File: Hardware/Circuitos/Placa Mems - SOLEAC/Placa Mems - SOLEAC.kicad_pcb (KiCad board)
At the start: 2 copper layers, 50 x 40 mm, 7 parts, among them J2 Conn_01x04, J6 Conn_01x02, Y1 MA40S4R

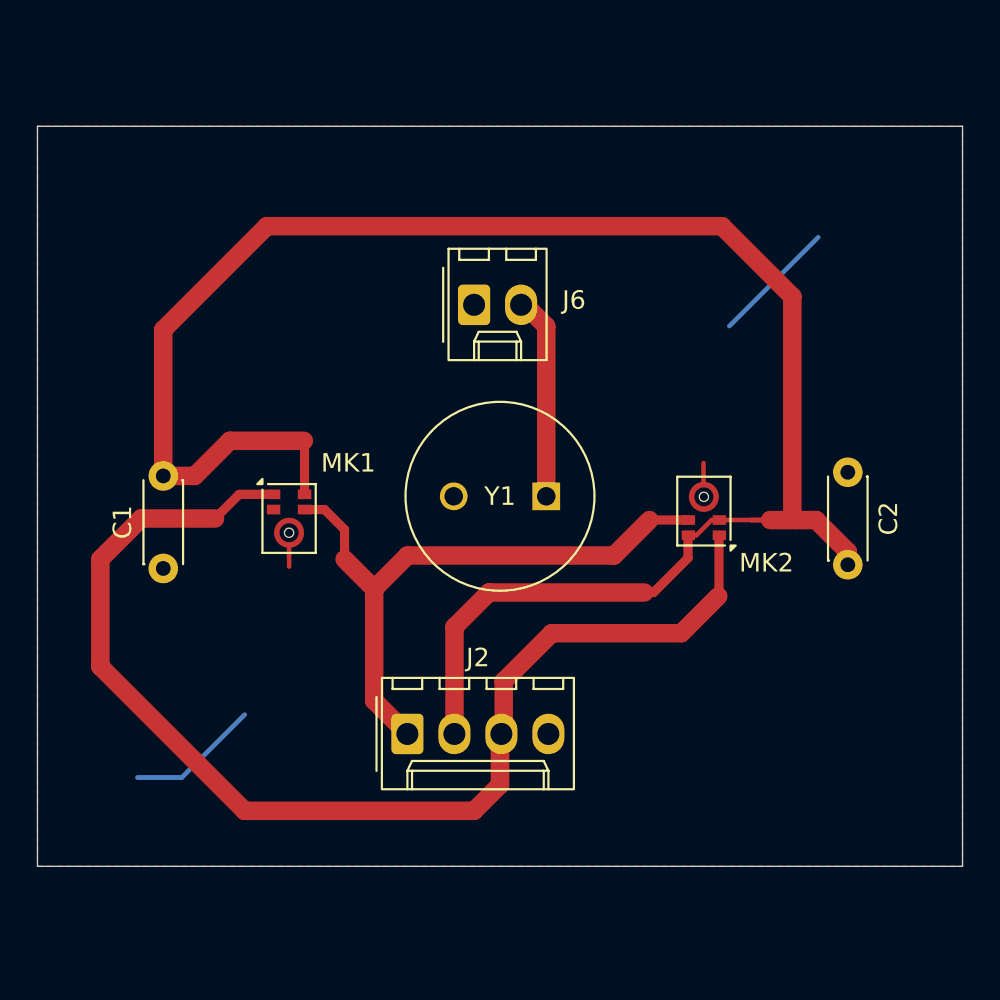
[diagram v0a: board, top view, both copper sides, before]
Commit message: Placa Mems - Margen de la placa
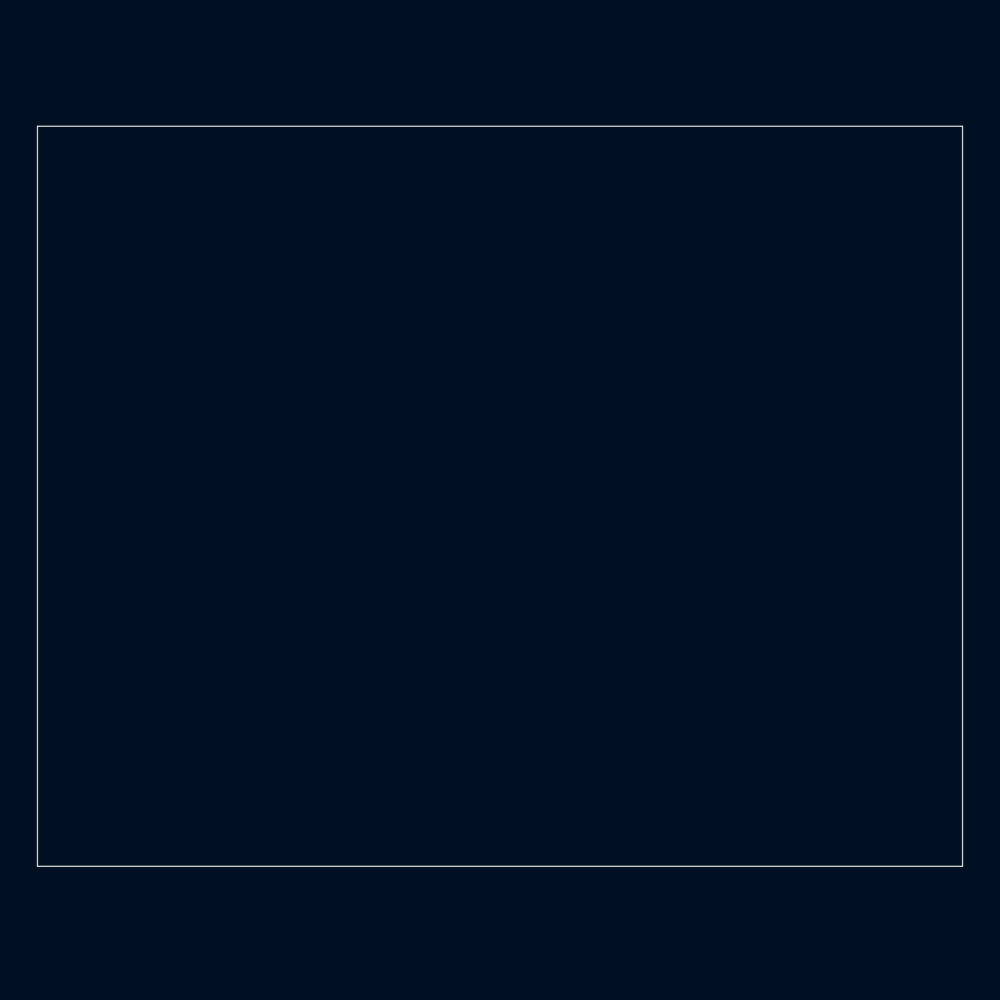
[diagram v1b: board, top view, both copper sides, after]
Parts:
- removed C1, C2: 100 nF, Capacitor_THT:C_Disc_D4.3mm_W1.9mm_P5.00mm
- removed J2: Conn_01x04, Connector_Molex:Molex_KK-254_AE-6410-04A_1x04_P2.54mm_Vertical
- removed J6: Conn_01x02, Connector_Molex:Molex_KK-254_AE-6410-02A_1x02_P2.54mm_Vertical
- removed MK1, MK2: SPH0641LU4H-1, Sensor_Audio:Knowles_LGA-5_3.5x2.65mm
- removed Y1: MA40S4R, Murata:MA4024R
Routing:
- net /3.3V: track 101.8 -> 0.00 mm
- net /GPIO40: track 64.5 -> 0.00 mm
- net /GPIO41: track 33.6 -> 0.00 mm
- net (no net): track 14.0 -> 0.00 mm
- net /entrada placa procesadora: track 10.8 -> 0.00 mm
- net Earth: track 2.34 -> 0.00 mm
- removed copper zone on F.Cu, net Earth
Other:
- board text removed: "Masa"

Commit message: Placa Mems - Componentes PCB
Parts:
- added C1: 100 nF, Capacitor_THT:C_Disc_D4.3mm_W1.9mm_P5.00mm, F.Cu at (32.0, 49.7)
- added C2: 100 nF, Capacitor_THT:C_Disc_D4.3mm_W1.9mm_P5.00mm, F.Cu at (69.0, 44.5)
- added J2: Conn_01x04, Connector_Molex:Molex_KK-254_AE-6410-04A_1x04_P2.54mm_Vertical, F.Cu at (45.2, 58.6)
- added J6: Conn_01x02, Connector_Molex:Molex_KK-254_AE-6410-02A_1x02_P2.54mm_Vertical, F.Cu at (48.8, 35.5)
- added MK1: SPH0641LU4H-1, Sensor_Audio:Knowles_LGA-5_3.5x2.65mm, F.Cu at (38.8, 47.0)
- added MK2: SPH0641LU4H-1, Sensor_Audio:Knowles_LGA-5_3.5x2.65mm, F.Cu at (61.2, 46.6)
- added Y1: MA40S4R, Murata:MA4024R, F.Cu at (50.2, 45.8)

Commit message: Placa Mems - Ruteo de PCB
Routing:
- net /3.3V: track 0.00 -> 101.8 mm
- net /GPIO40: track 0.00 -> 64.5 mm
- net /GPIO41: track 0.00 -> 33.6 mm
- net (no net): track 0.00 -> 14.0 mm
- net /entrada placa procesadora: track 0.00 -> 10.8 mm
- net Earth: track 0.00 -> 2.34 mm
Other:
- board text added: "Masa"

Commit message: Placa Mems - Zona de tierra
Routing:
- added copper zone on F.Cu, net Earth
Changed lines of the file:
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@@
 		(net "/entrada placa procesadora")
+	)
+	(zone
+		(net "Earth")
+		(layer "F.Cu")
+		(hatch edge 0.5)
+		(connect_pads
+			(clearance 0.5)
+		)
+		(min_thickness 0.25)
+		(fill yes
+			(thermal_gap 0.5)
+			(thermal_bridge_width 0.5)
+			(island_removal_mode 0)
+		)
+		(polygon
+			(pts
+				(xy 75.2 65.8) (xy 75.2 25.8) (xy 25.2 25.8) (xy 25.2 65.8)
+			)
+		)
 	)
 	(embedded_fonts no)

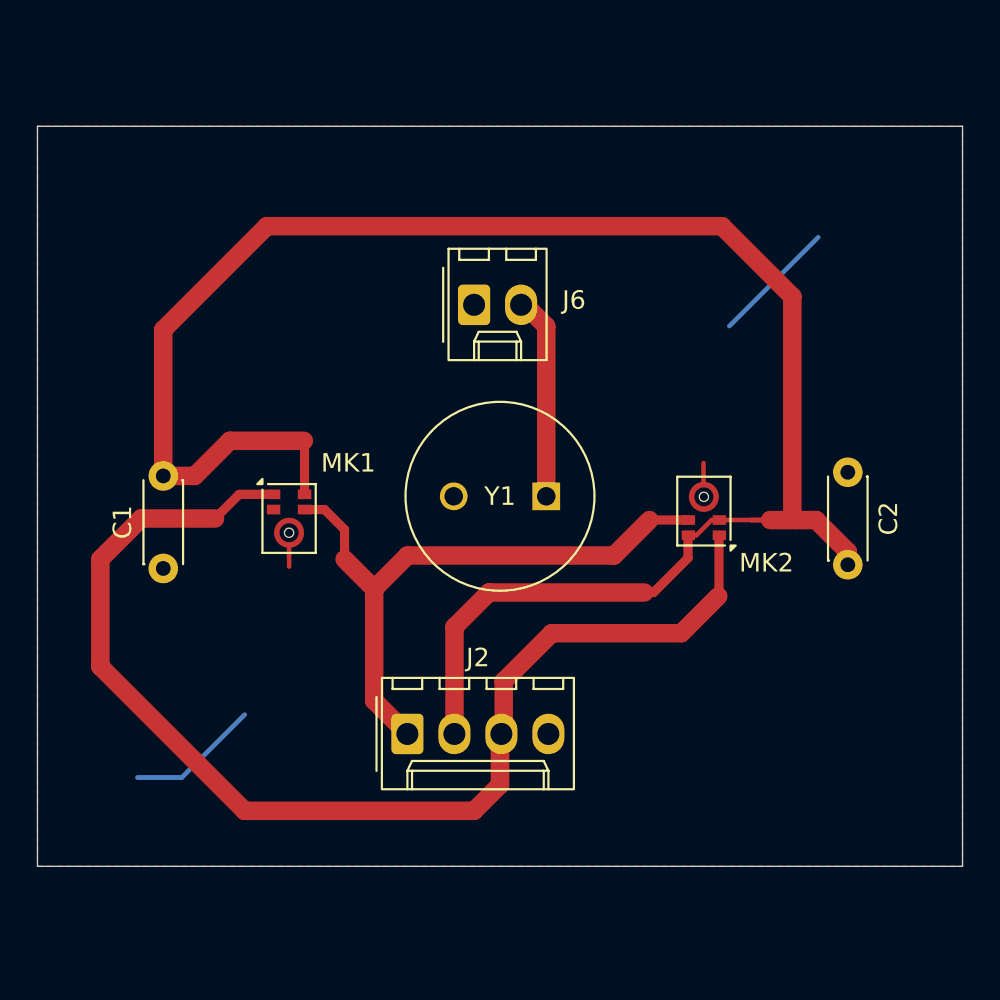
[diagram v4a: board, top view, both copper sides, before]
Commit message: Placa Mems - Poniendo plug ethernet
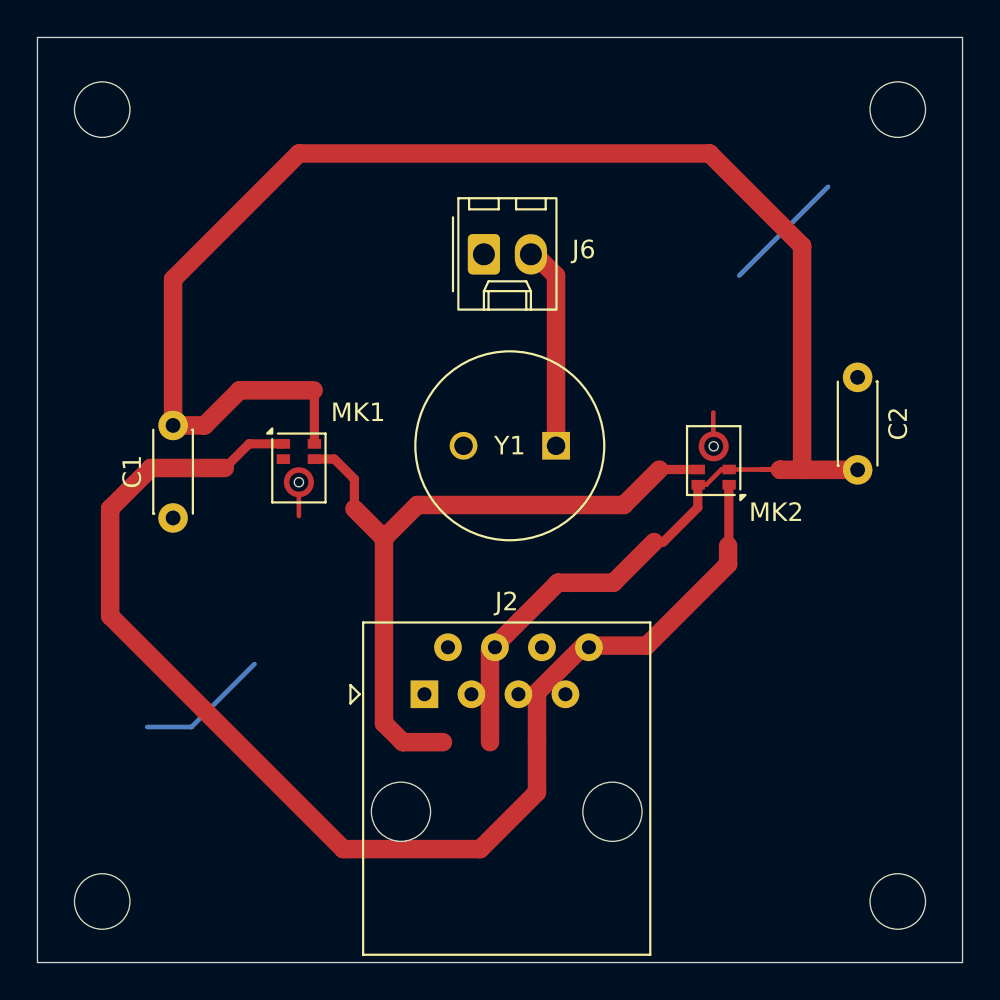
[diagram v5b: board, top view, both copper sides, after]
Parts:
- J2: footprint Connector_Molex:Molex_KK-254_AE-6410-04A_1x04_P2.54mm_Vertical -> Connector_RJ:RJ45_Amphenol_54602-x08_Horizontal
- moved C2 5.16 mm to (69.5, 39.4)
- moved C1 2.78 mm to (32.5, 47.0)
- moved J6 2.78 mm to (49.3, 32.7)
- moved MK2 2.78 mm to (61.8, 43.9)
- moved MK1 2.78 mm to (39.3, 44.3)
- moved Y1 2.78 mm to (50.7, 43.1)
- moved J2 2.33 mm to (46.1, 56.5)
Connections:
- net /GPIO40 renamed /GPIO38 D
- net /GPIO41 renamed /GPIO39 c
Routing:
- net /GPIO39 c: track 33.6 -> 38.6 mm
- net /GPIO38 D: track 64.5 -> 69.1 mm
- net /3.3V: track 101.8 -> 100.8 mm
- removed copper zone on F.Cu, net Earth
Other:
- board size 50 x 40 mm -> 50 x 50 mm
